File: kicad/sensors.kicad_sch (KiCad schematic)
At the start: 20 parts, among them J35 Sensors, J36 I2C 5V, U11 PCA9306D

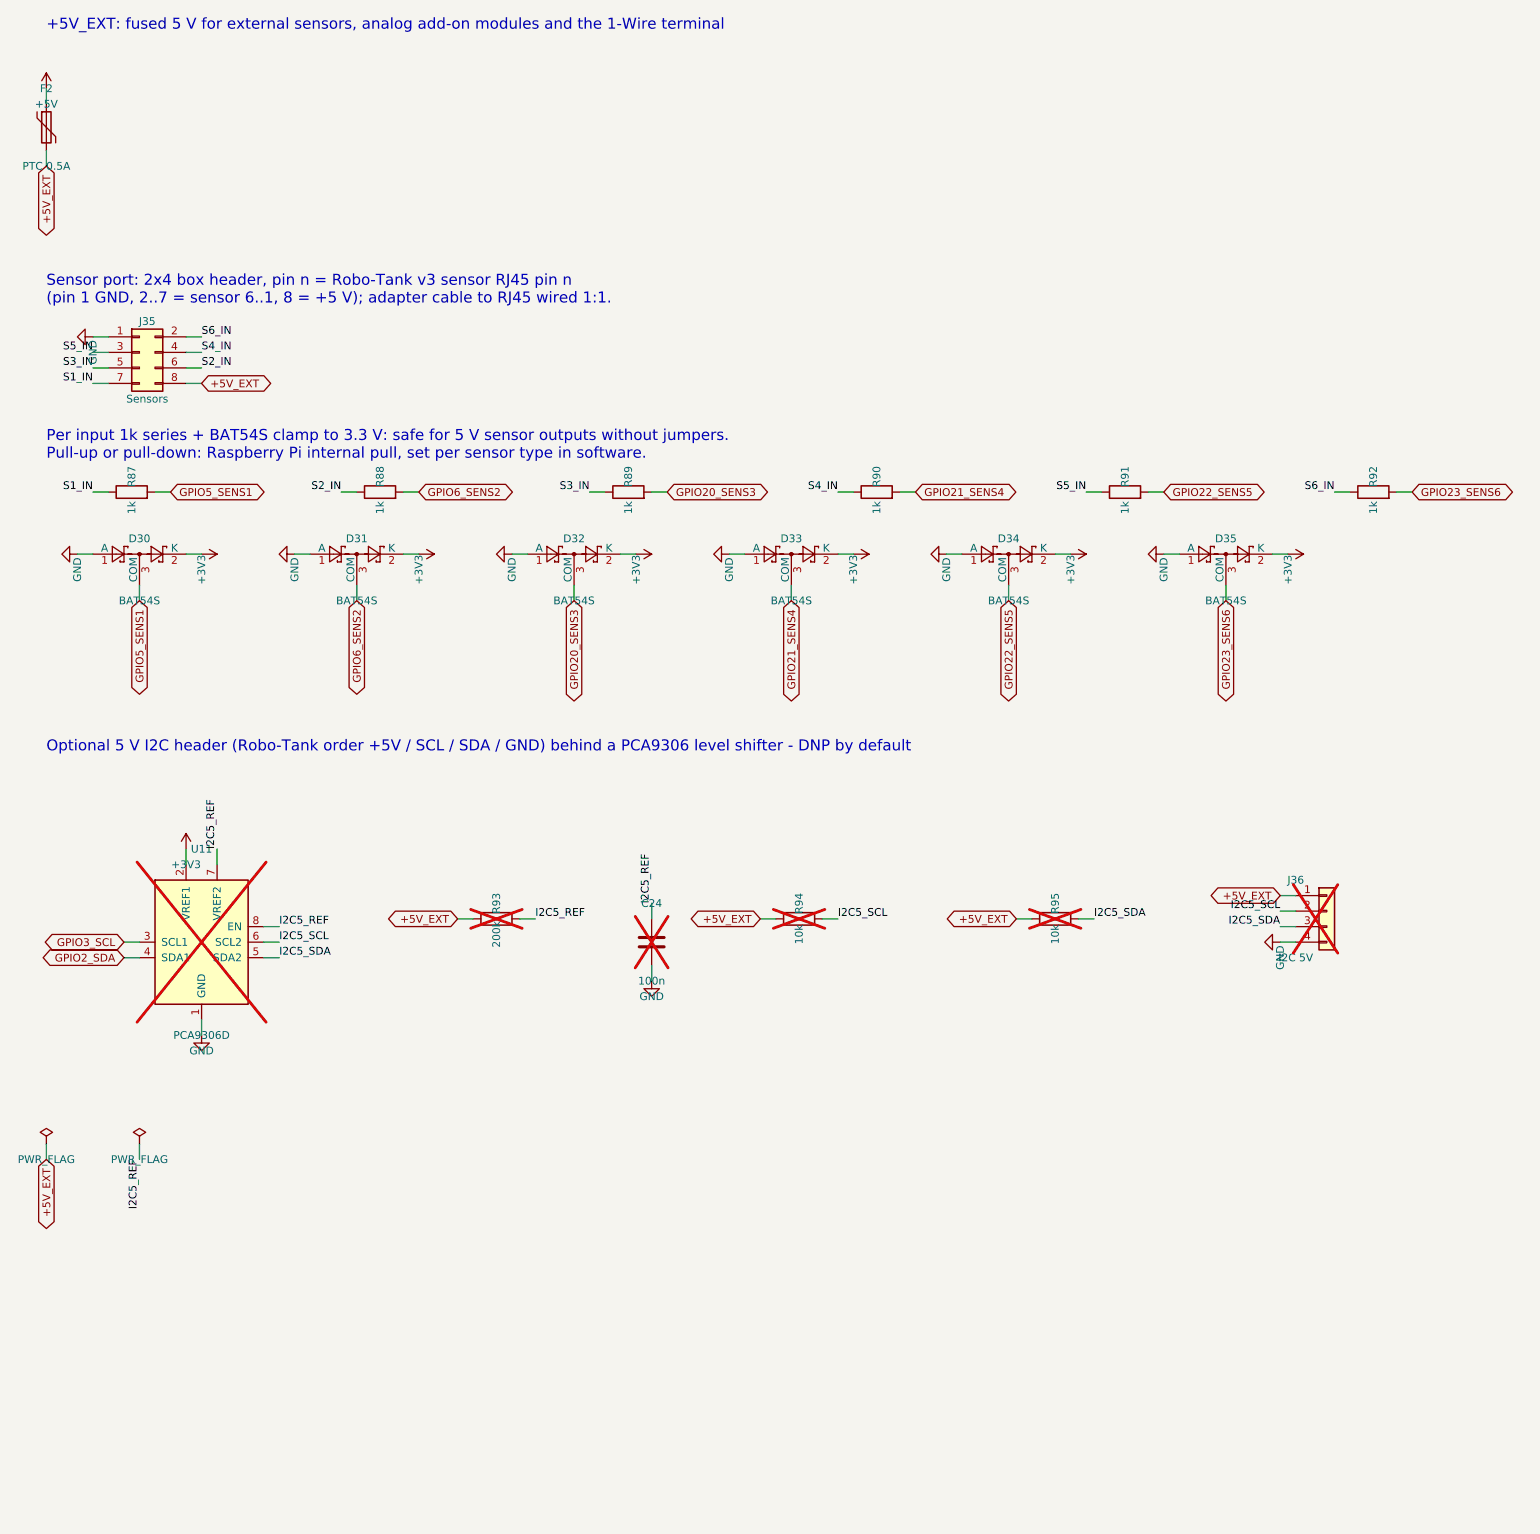
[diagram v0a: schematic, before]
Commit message: kicad: v2 space measures - feeder on power bar header, resistor arrays, 0603, TSSOP buffers
Feeder port dropped: power bar header pin 10 = +3V3_EXT (own AMS1117), any PCA #2 channel as signal; 30 series resistors as 8x 4x0603 arrays; new passives 0603; new 74HCT244 in TSSOP-20; flat parts may use the Pi zone, connectors anywhere else. ERC 0, DRC copper 0, parity 0.

Co-Authored-By: Claude Opus 5.5 <noreply@anthropic.com>
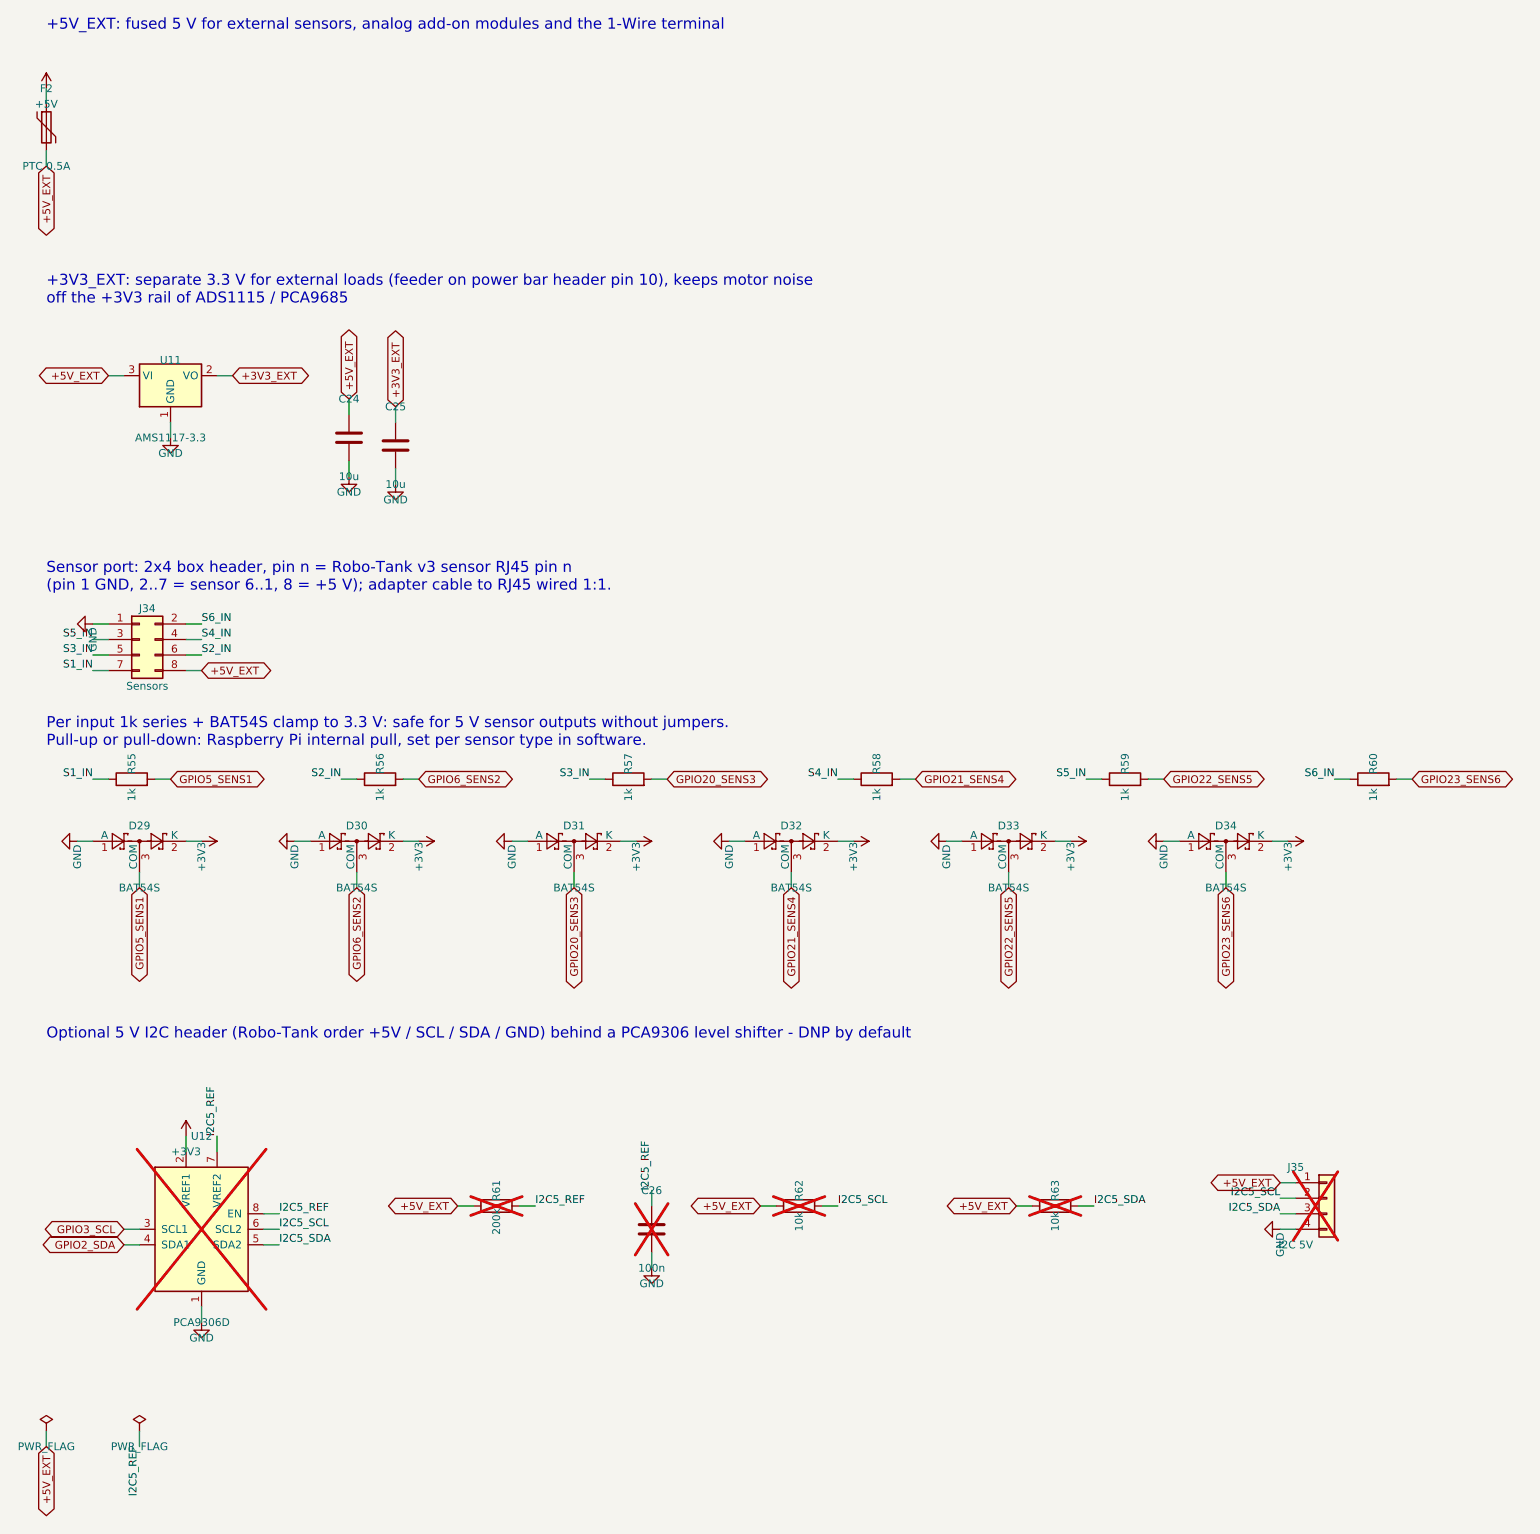
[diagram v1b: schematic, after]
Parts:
- removed D35: BAT54S, Package_TO_SOT_SMD:SOT-23, symbol Diode:BAT54S
- removed J35: Sensors, Connector_IDC:IDC-Header_2x04_P2.54mm_Vertical, symbol Connector_Generic:Conn_02x04_Odd_Even
- removed J36: I2C 5V, Connector_PinHeader_2.54mm:PinHeader_1x04_P2.54mm_Vertical, symbol Connector_Generic:Conn_01x04
- removed R87, R88, R89, R90, R91, R92: 1k, Resistor_SMD:R_0805_2012Metric, symbol Device:R
- removed R93: 200k, Resistor_SMD:R_0805_2012Metric, symbol Device:R
- removed R94, R95: 10k, Resistor_SMD:R_0805_2012Metric, symbol Device:R
- removed U11: PCA9306D, Package_SO:SOIC-8_3.9x4.9mm_P1.27mm, symbol Interface:PCA9306D
- added C25: 10u, Capacitor_SMD:C_0603_1608Metric, symbol Device:C
- added C26: 100n, Capacitor_SMD:C_0603_1608Metric, symbol Device:C
- added D29: BAT54S, Package_TO_SOT_SMD:SOT-23, symbol Diode:BAT54S
- added J34: Sensors, Connector_IDC:IDC-Header_2x04_P2.54mm_Vertical, symbol Connector_Generic:Conn_02x04_Odd_Even
- added J35: I2C 5V, Connector_PinHeader_2.54mm:PinHeader_1x04_P2.54mm_Vertical, symbol Connector_Generic:Conn_01x04
- added R55, R56, R57, R58, R59, R60: 1k, Resistor_SMD:R_0603_1608Metric, symbol Device:R
- added R61: 200k, Resistor_SMD:R_0603_1608Metric, symbol Device:R
- added R62, R63: 10k, Resistor_SMD:R_0603_1608Metric, symbol Device:R
- added U11: AMS1117-3.3, Package_TO_SOT_SMD:SOT-223-3_TabPin2, symbol Regulator_Linear:AMS1117-3.3
- added U12: PCA9306D, Package_SO:SOIC-8_3.9x4.9mm_P1.27mm, symbol Interface:PCA9306D
- C24: value 100n -> 10u; footprint Capacitor_SMD:C_0805_2012Metric -> Capacitor_SMD:C_0603_1608Metric; LCSC C49678 -> C19702; now fitted
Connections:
- net +3V3: now also D29.2 (K), U12.2 (VREF1)
- net +5V_EXT: now also C24.1, J34.8 (Pin_8), J35.1 (Pin_1), R61.1, R62.1, R63.1, U11.3 (VI)
- net GND: now also C25.2, C26.2, D29.1 (A), J34.1 (Pin_1), J35.4 (Pin_4), U11.1 (GND), U12.1 (GND)
- net GPIO20_SENS3: now also D31.3 (COM), R57.2; no longer D32.3 (COM)
- net GPIO21_SENS4: now also D32.3 (COM), R58.2; no longer D33.3 (COM)
- net GPIO22_SENS5: now also D33.3 (COM), R59.2; no longer D34.3 (COM)
- net GPIO23_SENS6: now also D34.3 (COM), R60.2
- net GPIO2_SDA: now also U12.4 (SDA1)
- net GPIO3_SCL: now also U12.3 (SCL1)
- net GPIO5_SENS1: now also D29.3 (COM), R55.2; no longer D30.3 (COM)
- net GPIO6_SENS2: now also D30.3 (COM), R56.2; no longer D31.3 (COM)
- net I2C5_REF: now also C26.1, R61.2, U12.7 (VREF2), U12.8 (EN); no longer C24.1
- net I2C5_SCL: now also J35.2 (Pin_2), R62.2, U12.6 (SCL2)
- net I2C5_SDA: now also J35.3 (Pin_3), R63.2, U12.5 (SDA2)
- net S1_IN: now also J34.7 (Pin_7), R55.1
- net S2_IN: now also J34.6 (Pin_6), R56.1
- net S3_IN: now also J34.5 (Pin_5), R57.1
- net S4_IN: now also J34.4 (Pin_4), R58.1
- net S5_IN: now also J34.3 (Pin_3), R59.1
- net S6_IN: now also J34.2 (Pin_2), R60.1
- new net +3V3_EXT: C25.1, U11.2 (VO)
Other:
- note added: "+3V3_EXT: separate 3.3 V for external loads (feeder on power bar header pin 10), keeps motor noise off the +3V3 rail of ADS1115 / PCA9685"

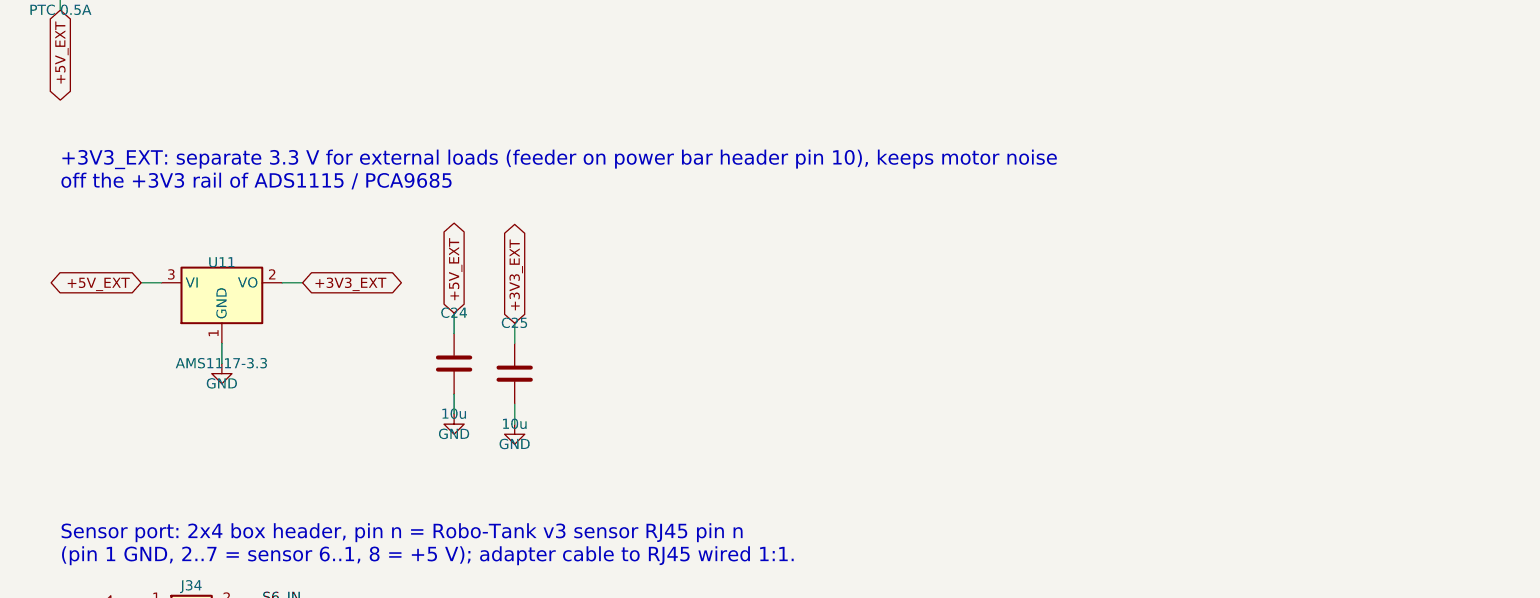
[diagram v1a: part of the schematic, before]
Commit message: kicad: pin headers for 1-Wire, ADC and floats; connectivity-driven re-placement
J19, ADC sockets (J36/J37/J26/J27, 3x4 grid) and floats J30/J31 are pin headers now. All footprints placed on the board (big connectors first, flat parts allowed under the Pi, user-placed U10/RN5/J32/U11 and user routing kept): signal ratsnest 7824 -> 4450 mm, crossings 1776 -> 862. ERC 0, DRC copper 0, parity 0.

Co-Authored-By: Claude Opus 5.5 <noreply@anthropic.com>
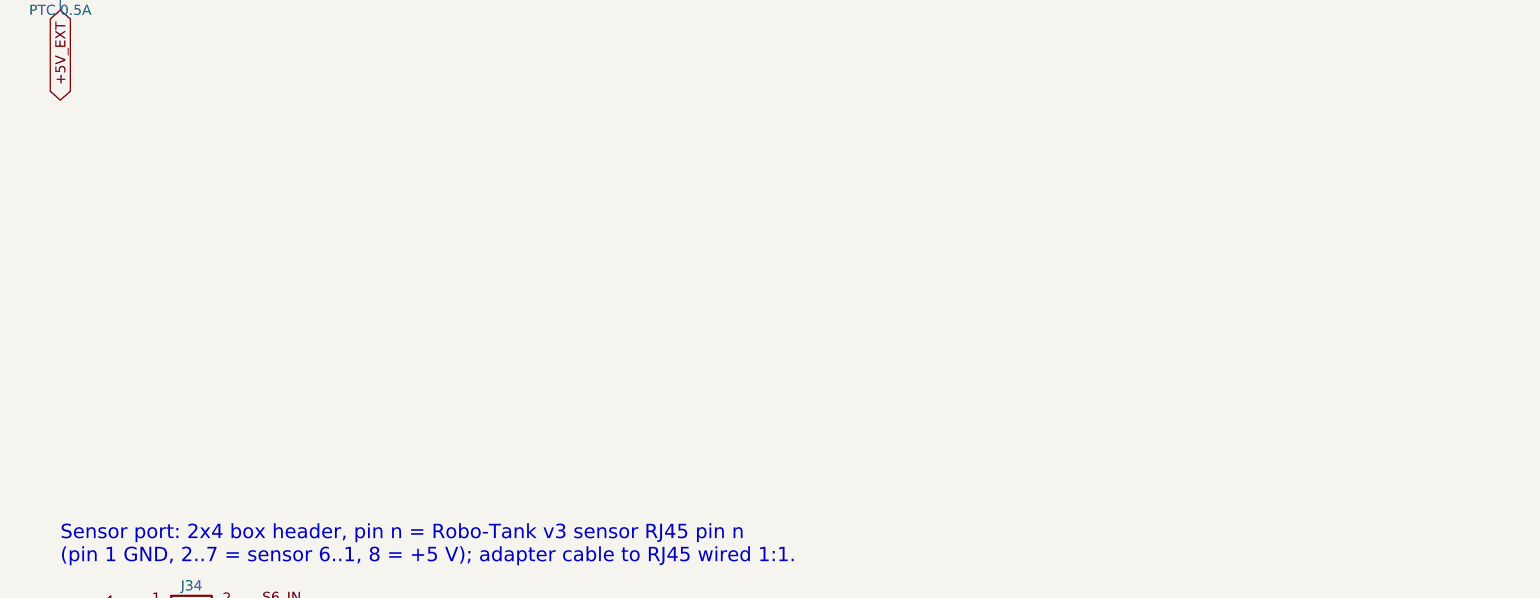
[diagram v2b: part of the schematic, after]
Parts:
- removed C24, C25: 10u, Capacitor_SMD:C_0603_1608Metric, symbol Device:C
- removed U11: AMS1117-3.3, Package_TO_SOT_SMD:SOT-223-3_TabPin2, symbol Regulator_Linear:AMS1117-3.3
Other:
- note removed: "+3V3_EXT: separate 3.3 V for external loads (feeder on power bar header pin 10), keeps motor noise off the +3V3 rail of ADS1115 / PCA9685"
